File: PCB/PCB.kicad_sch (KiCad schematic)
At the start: 0 parts

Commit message: feat: Update PCB with size and pads
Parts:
- added GND: Ground, TestPoint:TestPoint_THTPad_2.0x2.0mm_Drill1.0mm, symbol Connector:TestPoint
- added SN1: Channel 1, TestPoint:TestPoint_THTPad_2.0x2.0mm_Drill1.0mm, symbol Connector:TestPoint
- added SN2: Channel 2, TestPoint:TestPoint_THTPad_2.0x2.0mm_Drill1.0mm, symbol Connector:TestPoint
- added SN3: Channel 3, TestPoint:TestPoint_THTPad_2.0x2.0mm_Drill1.0mm, symbol Connector:TestPoint
- added VCC: Power, TestPoint:TestPoint_THTPad_2.0x2.0mm_Drill1.0mm, symbol Connector:TestPoint

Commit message: feat: add components
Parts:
- added U1: STM32G031F6P6, Package_SO:TSSOP-20_4.4x6.5mm_P0.65mm, symbol Nano2A:STM32G031F6P6
- added U2: XN297L, Package_SO:SSOP-16_3.9x4.9mm_P0.635mm, symbol Nano2A:XN297L
- added U3: HT7333-3.3V, Package_TO_SOT_SMD:SOT-89-3, symbol Nano2A:HT7333
- GND1: renamed from GND; footprint TestPoint:TestPoint_THTPad_2.0x2.0mm_Drill1.0mm -> TestPoint:TestPoint_THTPad_1.0x1.0mm_Drill0.5mm
- SN1, SN2, SN3: footprint TestPoint:TestPoint_THTPad_2.0x2.0mm_Drill1.0mm -> TestPoint:TestPoint_THTPad_1.0x1.0mm_Drill0.5mm
- VCC1: renamed from VCC; footprint TestPoint:TestPoint_THTPad_2.0x2.0mm_Drill1.0mm -> TestPoint:TestPoint_THTPad_1.0x1.0mm_Drill0.5mm

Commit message: feat: added all components
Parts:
- added C1, C2, C3, C4, C5, C6: C, Capacitor_SMD:C_0402_1005Metric, symbol Device:C
- added C7: C, Capacitor_SMD:C_0603_1608Metric, symbol Device:C
- added L1: L, Inductor_SMD:L_0402_1005Metric, symbol Device:L
- added R1, R2, R3: R, Resistor_SMD:R_0402_1005Metric, symbol Device:R
- added Y1: Crystal, Crystal:Crystal_SMD_3225-4Pin_3.2x2.5mm, symbol Device:Crystal

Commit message: feat: rename channels and organise
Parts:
- added R4: R, Resistor_SMD:R_0402_1005Metric, symbol Device:R
- added TP1: SWDIO, TestPoint:TestPoint_Pad_D1.0mm, symbol Connector:TestPoint
- added TP2: SWCLK, TestPoint:TestPoint_Pad_D1.0mm, symbol Connector:TestPoint
- renumbered SN1 to CH1, SN2 to CH2, SN3 to CH3
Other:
- moved on the sheet: CH2, CH3, U1, VCC1

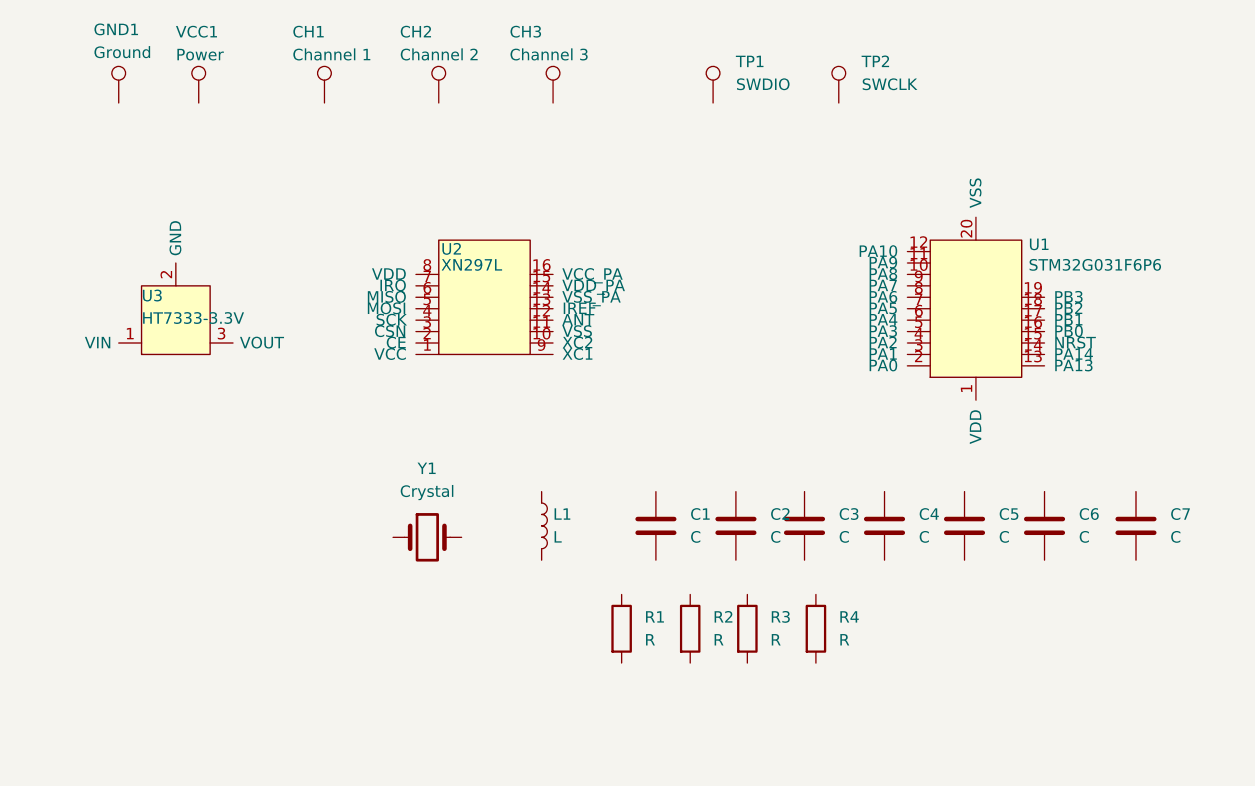
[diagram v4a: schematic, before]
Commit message: feat: update PCB traces and move components
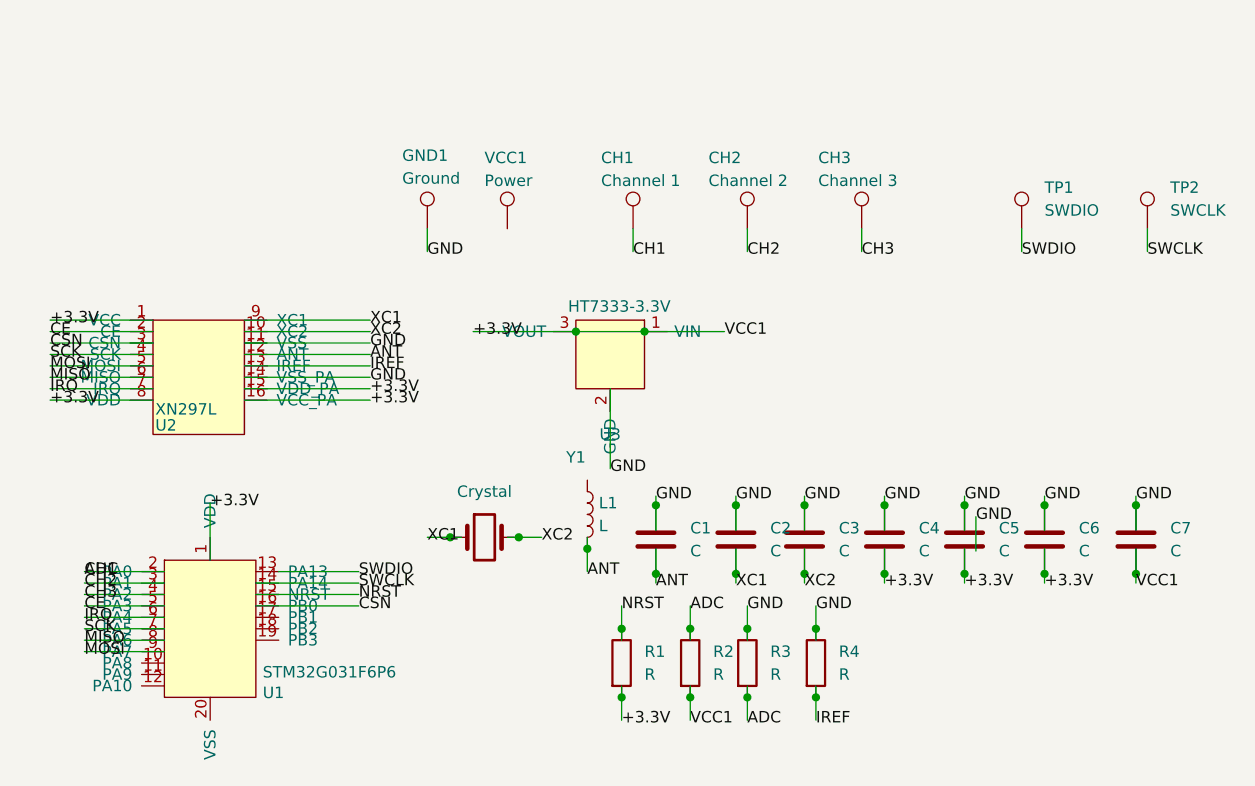
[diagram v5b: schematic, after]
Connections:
- net ADC: now reaches CH1.1
- net ADC: now also R2.1, R3.2, U1.2 (PA0)
- net SWDIO: now reaches TP1.1
- net XC1: now reaches Y1.1
- net XC1: now also C2.2, U2.9 (XC1)
- net XC2: now reaches Y1.2
- net XC2: now also C3.2, U2.10 (XC2)
- net GND: now reaches C3.1
- net GND: now also C1.1, C2.1, C4.1, C5.1, C6.1, C7.1, GND1.1, R3.1, R4.1, U2.11 (VSS), U2.14 (VSS_PA), U3.2 (GND)
- net +3.3V: now reaches C4.2
- net +3.3V: now also C5.2, C6.2, C7.2, R1.2, R2.2, U1.1 (VDD), U2.1 (VCC), U2.15 (VDD_PA), U2.16 (VCC_PA), U2.8 (VDD), U3.1 (VIN), U3.3 (VOUT)
- net IREF: now reaches R4.2
- net IREF: now also U2.13 (IREF)
- net CH2: now reaches CH2.1
- net CH2: now also U1.3 (PA1)
- net SWCLK: now reaches TP2.1
- net SWCLK: now also U1.14 (PA14)
- net NRST: now reaches U1.15 (NRST)
- net NRST: now also R1.1
- net CSN: now reaches U1.16 (PB0)
- net CSN: now also U2.3 (CSN)
- net CH3: now reaches U1.4 (PA2)
- net CH3: now also CH3.1
- net CE: now reaches U1.5 (PA3)
- net CE: now also U2.2 (CE)
- net IRQ: now reaches U1.6 (PA4)
- net IRQ: now also U2.7 (IRQ)
- net SCK: now reaches U1.7 (PA5)
- net SCK: now also U2.4 (SCK)
- net MISO: now reaches U1.8 (PA6)
- net MISO: now also U2.6 (MISO)
- net MOSI: now reaches U1.9 (PA7)
- net MOSI: now also U2.5 (MOSI)
- net ANT: now reaches U2.12 (ANT)
- net ANT: now also C1.2, L1.2
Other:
- moved on the sheet: C1, C2, C3, C4, C5, C6, C7, CH1, CH2, CH3, GND1, L1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

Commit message: fix: add component values
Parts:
- C1: value C -> 2.7pF
- C2, C3: value C -> 22pF
- C4, C5, C6: value C -> 100nF
- C7: value C -> 10µF
- L1: value L -> 2.2nH
- R1, R2: value R -> 10k
- R3: value R -> 1.8k
- R4: value R -> 22k
- Y1: value Crystal -> 16MHz
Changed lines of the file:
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@@
 			)
 		)
-		(property "Value" "Crystal"
+		(property "Value" "16MHz"
 			(at 64.77 66.04 0)
 			(show_name no)
@@
 			)
 		)
-		(property "Value" "C"
+		(property "Value" "22pF"
 			(at 104.14 72.6399 0)
 			(show_name no)
@@
 			)
 		)
-		(property "Value" "C"
+		(property "Value" "100nF"
 			(at 113.03 72.6399 0)
 			(show_name no)
@@
 			)
 		)
-		(property "Value" "R"
+		(property "Value" "22k"
 			(at 104.14 86.3599 0)
 			(show_name no)
@@
 			)
 		)
-		(property "Value" "R"
+		(property "Value" "1.8k"
 			(at 96.52 86.3599 0)
 			(show_name no)
@@
 			)
 		)
-		(property "Value" "C"
+		(property "Value" "100nF"
 			(at 130.81 72.6399 0)
 			(show_name no)
@@
 			)
 		)
-		(property "Value" "R"
+		(property "Value" "10k"
 			(at 82.55 86.3599 0)
 			(show_name no)
@@
 			)
 		)
-		(property "Value" "R"
+		(property "Value" "10k"
 			(at 90.17 86.3599 0)
 			(show_name no)
@@
 			)
 		)
-		(property "Value" "L"
+		(property "Value" "2.2nH"
 			(at 77.47 69.8499 0)
 			(show_name no)
@@
 			)
 		)
-		(property "Value" "C"
+		(property "Value" "100nF"
 			(at 121.92 72.6399 0)
 			(show_name no)
@@
 			)
 		)
-		(property "Value" "C"
+		(property "Value" "22pF"
 			(at 96.52 72.6399 0)
 			(show_name no)
@@
 			)
 		)
-		(property "Value" "C"
+		(property "Value" "2.7pF"
 			(at 87.63 72.6399 0)
 			(show_name no)
@@
 			)
 		)
-		(property "Value" "C"
+		(property "Value" "10µF"
 			(at 140.97 72.6399 0)
 			(show_name no)

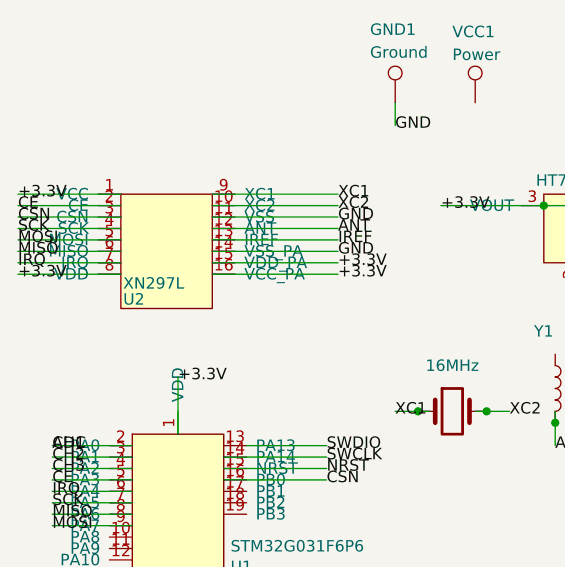
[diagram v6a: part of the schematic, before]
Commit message: feat: add LTSC part numbers
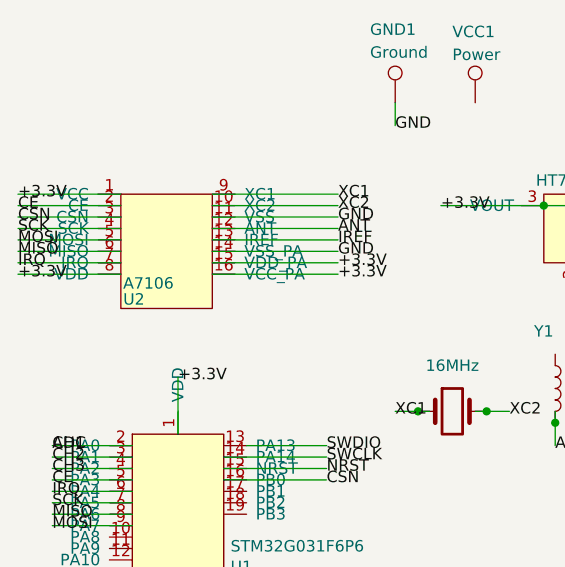
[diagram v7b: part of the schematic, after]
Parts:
- C1: LCSC (none) -> C438213
- C2, C3: LCSC (none) -> C1555
- C4, C5, C6: LCSC (none) -> C41851
- C7: LCSC (none) -> C19702
- L1: LCSC (none) -> C91240
- R1, R2: LCSC (none) -> C843837
- R3: LCSC (none) -> C137909
- R4: LCSC (none) -> C144778
- U1: LCSC (none) -> C529333
- U2: value XN297L -> A7106; LCSC (none) -> —
- U3: LCSC (none) -> C84207
- Y1: LCSC (none) -> C12668
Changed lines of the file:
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@@
+			)
+		)
+		(property "LCSC" "C12668"
+			(at 64.77 71.12 0)
+			(hide yes)
+			(show_name no)
+			(do_not_autoplace no)
+			(effects
+				(font
+					(size 1.27 1.27)
+				)
 			)
 		)
@@
 			)
 		)
+		(property "LCSC" "C1555"
+			(at 100.33 71.37 0)
+			(hide yes)
+			(show_name no)
+			(do_not_autoplace no)
+			(effects
+				(font
+					(size 1.27 1.27)
+				)
+			)
+		)
 		(pin "1"
 		)
@@
 			)
 		)
+		(property "LCSC" "C41851"
+			(at 109.22 71.37 0)
+			(hide yes)
+			(show_name no)
+			(do_not_autoplace no)
+			(effects
+				(font
+					(size 1.27 1.27)
+				)
+			)
+		)
 		(pin "1"
 		)
@@
 			)
 		)
+		(property "LCSC" "C144778"
+			(at 101.6 85.09 0)
+			(hide yes)
+			(show_name no)
+			(do_not_autoplace no)
+			(effects
+				(font
+					(size 1.27 1.27)
+				)
+			)
+		)
 		(pin "2"
 		)
@@
 			)
 		)
+		(property "LCSC" "C137909"
+			(at 93.98 85.09 0)
+			(hide yes)
+			(show_name no)
+			(do_not_autoplace no)
+			(effects
+				(font
+					(size 1.27 1.27)
+				)
+			)
+		)
 		(pin "2"
 		)
@@
 			)
 		)
+		(property "LCSC" "C529333"
+			(at 29.21 73.66 0)
+			(hide yes)
+			(show_name no)
+			(do_not_autoplace no)
+			(effects
+				(font
+					(size 1.27 1.27)
+				)
+			)
+		)
 		(pin "1"
 		)
@@
 		(property "Description" ""
 			(at 82.55 46.99 0)
+			(show_name no)
+			(do_not_autoplace no)
+			(effects
+				(font
+					(size 1.27 1.27)
+				)
+			)
+		)
+		(property "LCSC" "C84207"
+			(at 82.55 46.99 0)
+			(hide yes)
 			(show_name no)
 			(do_not_autoplace no)
@@
 			)
 		)
+		(property "LCSC" "C41851"
+			(at 127 71.37 0)
+			(hide yes)
+			(show_name no)
+			(do_not_autoplace no)
+			(effects
+				(font
+					(size 1.27 1.27)
+				)
+			)
+		)
 		(pin "1"
 		)
@@
 			)
 		)
+		(property "LCSC" "C843837"
+			(at 80.01 85.09 0)
+			(hide yes)
+			(show_name no)
+			(do_not_autoplace no)
+			(effects
+				(font
+					(size 1.27 1.27)
+				)
+			)
+		)
 		(pin "2"
 		)
@@
 			)
 		)
+		(property "LCSC" "C843837"
+			(at 87.63 85.09 0)
+			(hide yes)
+			(show_name no)
+			(do_not_autoplace no)
+			(effects
+				(font
+					(size 1.27 1.27)
+				)
+			)
+		)
 		(pin "2"
 		)
@@
 			)
 		)
-		(property "Value" "XN297L"
+		(property "Value" "A7106"
 			(at 28.194 56.896 0)
 			(show_name no)
@@
 		(property "Description" ""
 			(at 27.94 46.99 0)
+			(show_name no)
+			(do_not_autoplace no)
+			(effects
+				(font
+					(size 1.27 1.27)
+				)
+			)
+		)
+		(property "LCSC" "—"
+			(at 27.94 46.99 0)
+			(hide yes)
 			(show_name no)
 			(do_not_autoplace no)
@@
 			)
 		)
+		(property "LCSC" "C91240"
+			(at 76.2 68.58 0)
+			(hide yes)
+			(show_name no)
+			(do_not_autoplace no)
+			(effects
+				(font
+					(size 1.27 1.27)
+				)
+			)
+		)
 		(pin "1"
 		)
@@
 			)
 		)
+		(property "LCSC" "C41851"
+			(at 118.11 71.37 0)
+			(hide yes)
+			(show_name no)
+			(do_not_autoplace no)
+			(effects
+				(font
+					(size 1.27 1.27)
+				)
+			)
+		)
 		(pin "1"
 		)
@@
 			)
 		)
+		(property "LCSC" "C1555"
+			(at 92.71 71.37 0)
+			(hide yes)
+			(show_name no)
+			(do_not_autoplace no)
+			(effects
+				(font
+					(size 1.27 1.27)
+				)
+			)
+		)
 		(pin "1"
 		)
@@
 			)
 		)
+		(property "LCSC" "C438213"
+			(at 83.82 71.37 0)
+			(hide yes)
+			(show_name no)
+			(do_not_autoplace no)
+			(effects
+				(font
+					(size 1.27 1.27)
+				)
+			)
+		)
 		(pin "1"
 		)
@@
 			(at 137.16 71.37 0)
 			(hide yes)
+			(show_name no)
+			(do_not_autoplace no)
+			(effects
+				(font
+					(size 1.27 1.27)
+				)
+			)
+		)
+		(property "LCSC" "C19702"
+			(at 137.16 71.37 0)
+			(hide yes)

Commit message: feat: Add symbol libraries for A7106
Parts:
- U2: footprint Package_SO:SSOP-16_3.9x4.9mm_P0.635mm -> Package_DFN_QFN:QFN-20-1EP_4x4mm_P0.5mm_EP2.5x2.5mm; symbol Nano2A:XN297L -> Nano2A:A7106
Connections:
- net +3.3V: no longer U2.1 (VCC), U2.15 (VDD_PA), U2.16 (VCC_PA), U2.8 (VDD)
- net ANT: no longer U2.12 (ANT)
- net CE: no longer U2.2 (CE)
- net CSN: no longer U2.3 (CSN)
- net GND: no longer U2.11 (VSS), U2.14 (VSS_PA)
- net IREF: no longer U2.13 (IREF)
- net IRQ: no longer U2.7 (IRQ)
- net MISO: no longer U2.6 (MISO)
- net MOSI: no longer U2.5 (MOSI)
- net SCK: no longer U2.4 (SCK)
- net XC1: no longer U2.9 (XC1)
- net XC2: no longer U2.10 (XC2)
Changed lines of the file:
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@@
 	)
 	(symbol
-		(lib_id "Nano2A:XN297L")
+		(lib_id "Nano2A:A7106")
 		(at 27.94 46.99 0)
 		(mirror x)
@@
 			)
 		)
-		(property "Footprint" "Package_SO:SSOP-16_3.9x4.9mm_P0.635mm"
+		(property "Footprint" "Package_DFN_QFN:QFN-20-1EP_4x4mm_P0.5mm_EP2.5x2.5mm"
 			(at 38.1 46.99 0)
 			(hide yes)
@@
 		(pin "16"
 		)
+		(pin "17"
+		)
+		(pin "18"
+		)
+		(pin "19"
+		)
+		(pin "20"
+		)
 		(instances
